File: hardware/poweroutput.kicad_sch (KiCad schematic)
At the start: 17 parts, among them J4 DG142R-5.08-02P-14-00AH, J5 108-0902-001, J6 108-0903-001, Q5 60V 4mR TBD, Q6 60V 4mR TBD, U12 AP74502Q

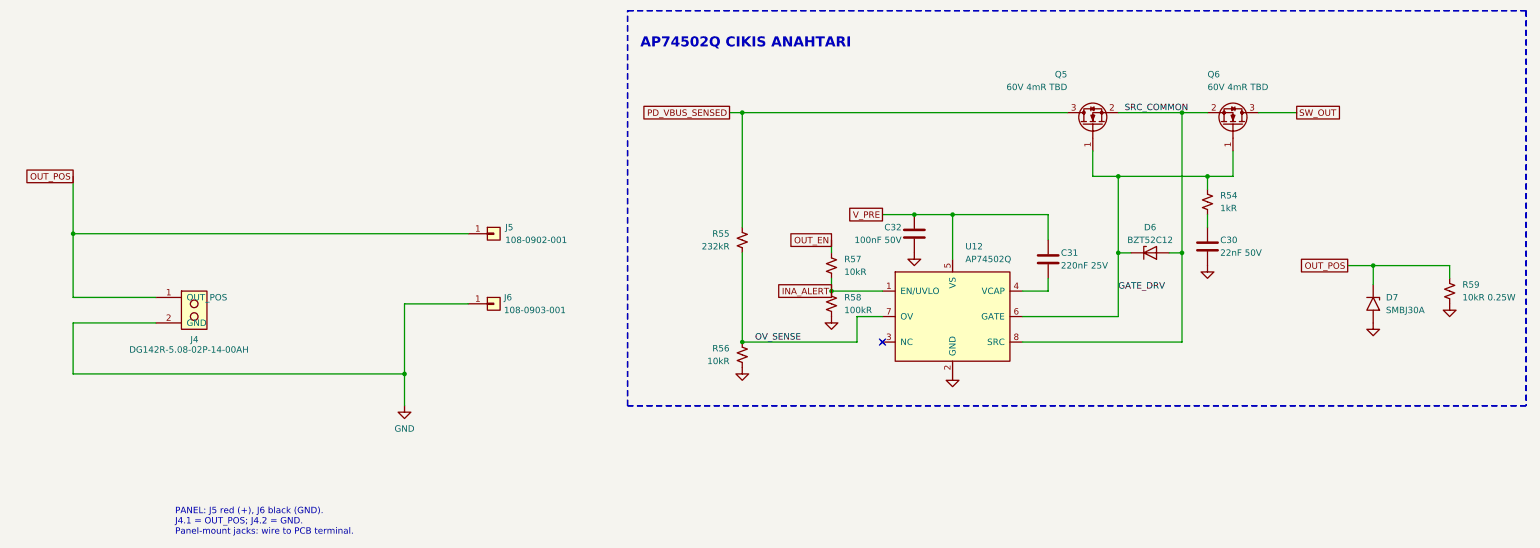
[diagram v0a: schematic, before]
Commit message: poweroutput: panel konnektör grubunu yeniden çiz
J4 aynalandı, OUT_POS/GND tek düz hat; grup çerçeve ve başlık aldı.
DG142R pin adları gövdeye biniyordu, kütüphane ve önbellekte gizlendi.
Blok B çerçevesinin yinelenen kopyası silindi. Netlist değişmedi.

Co-Authored-By: Claude Opus 5 <noreply@anthropic.com>
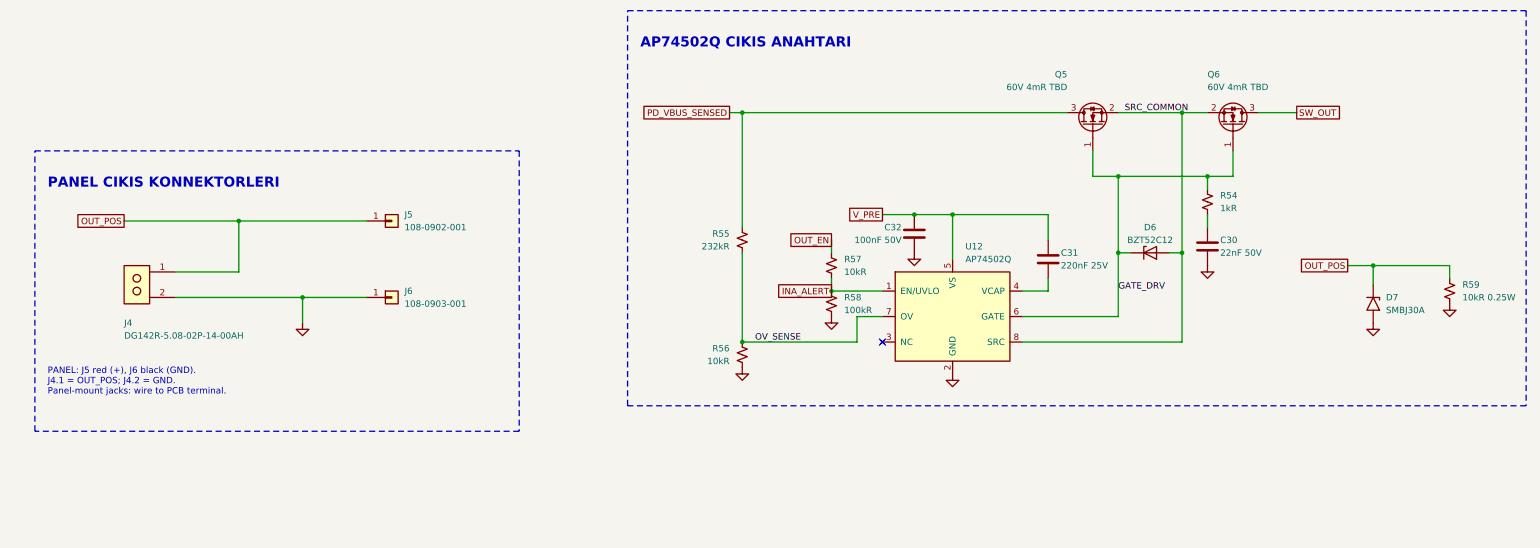
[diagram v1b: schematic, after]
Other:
- note added: "PANEL CIKIS KONNEKTORLERI"
- moved on the sheet: J5, J6
